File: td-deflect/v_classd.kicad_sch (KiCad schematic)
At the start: 34 parts, among them J8 Conn_01x02_Male, Q15 BSC600N25NS3GATMA1CT-ND, Q16 BSC600N25NS3GATMA1CT-ND, Q20 BSC600N25NS3GATMA1CT-ND, Q21 BSC600N25NS3GATMA1CT-ND, U34 IRS2005S, U35 IRS2005S, U36 MAX9919F, U37 MAX9919F

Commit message: fix drc errors
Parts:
- J8: symbol Connector:Conn_01x02_Male -> Connector:Conn_01x02_Pin
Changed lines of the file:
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@@
     )
   )
-  (symbol (lib_id "Connector:Conn_01x02_Male") (at 190.5 77.47 0) (mirror y) (unit 1)
+  (symbol (lib_id "Connector:Conn_01x02_Pin") (at 190.5 77.47 0) (mirror y) (unit 1)
     (in_bom yes) (on_board yes) (dnp no)
     (property "Reference" "J8" (at 187.7568 72.8726 0)

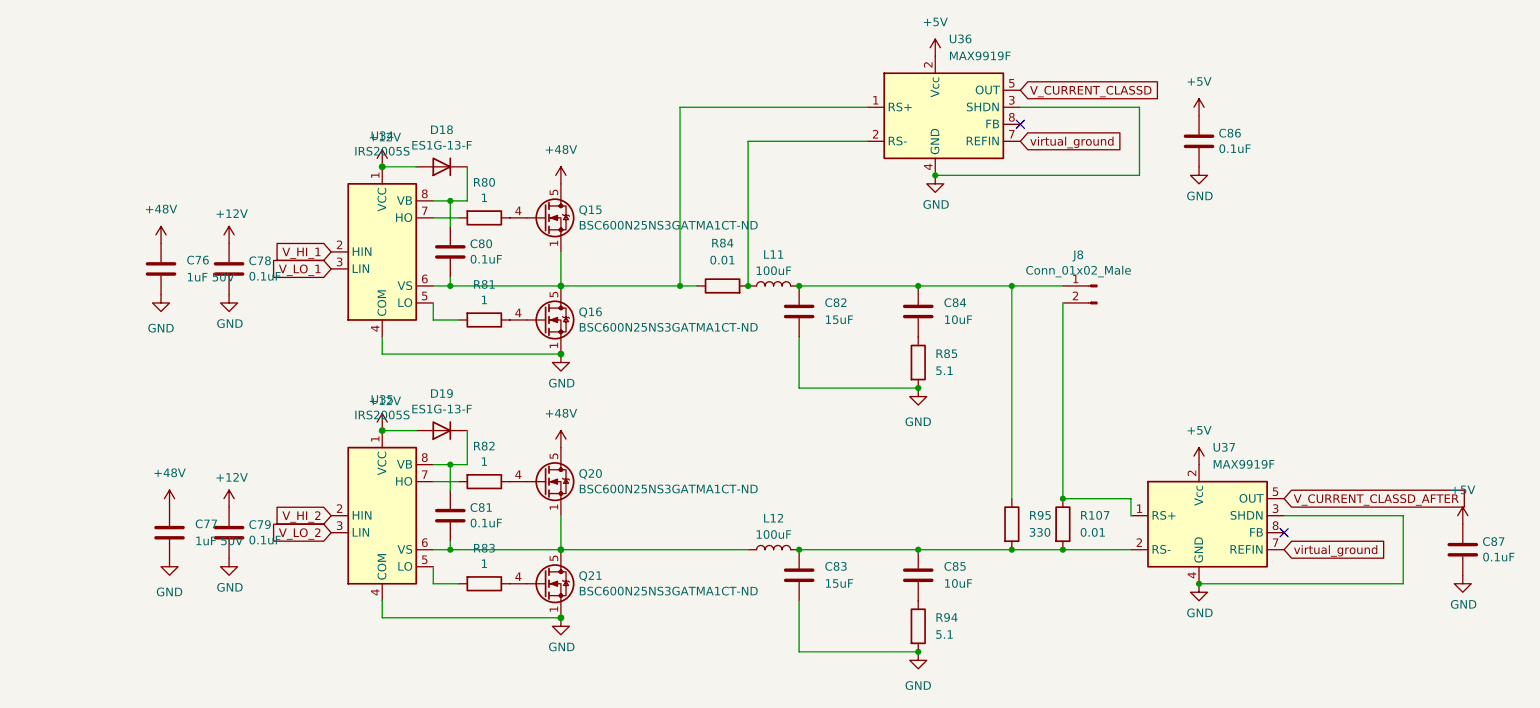
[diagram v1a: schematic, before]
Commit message: fix remaining erc errors
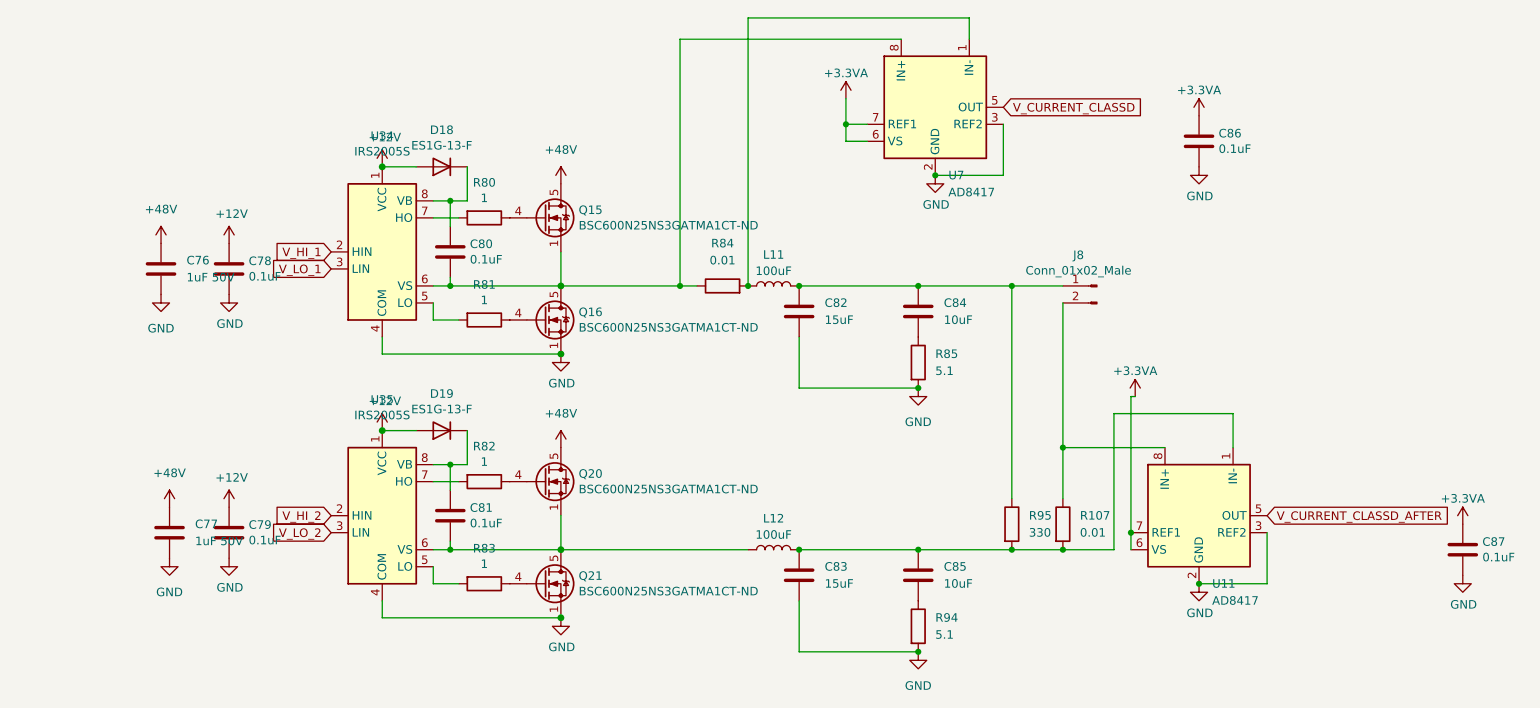
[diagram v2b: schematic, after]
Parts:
- removed U36, U37: MAX9919F, Package_SO:SOIC-8-1EP_3.9x4.9mm_P1.27mm_EP2.41x3.3mm, symbol td-crt:MAX9919F
- added U11, U7: AD8417, symbol Amplifier_Current:AD8417
- D18, D19: footprint Diode_SMD:D_SMA -> Diode_THT:D_DO-41_SOD81_P10.16mm_Horizontal
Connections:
- net GND: now also U11.2 (GND), U11.3 (REF2), U7.2 (GND), U7.3 (REF2)
- net V_CURRENT_CLASSD: now also U7.5 (OUT)
- net V_CURRENT_CLASSD_AFTER: now also U11.5 (OUT)
- net at C83.1, C85.1, L12.2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: now also U11.1 (IN-)
- net at C80.2, Q15.1 (S), Q15.2 (S)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: now also U7.8 (IN+)
- net at L11.1, R84.2: now also U7.1 (IN-)
- net at J8.2 (Pin_2), R107.1: now also U11.8 (IN+)
- net +5V renamed +3.3VA
- net +3.3VA: now also U11.6 (VS), U11.7 (REF1), U7.6 (VS), U7.7 (REF1)
- no-connect marks 2 -> 0

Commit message: more layout work
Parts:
- D18, D19: value ES1G-13-F -> 1N4148W-TP; footprint Diode_THT:D_DO-41_SOD81_P10.16mm_Horizontal -> Diode_SMD:D_SOD-123; Digikey ES1G-FDICT-ND -> 1N4148WTPMSCT-ND
- U11, U7: footprint (none) -> Package_SO:SOIC-8_3.9x4.9mm_P1.27mm
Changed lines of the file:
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@@
       (effects (font (size 1.27 1.27)))
     )
-    (property "Value" "ES1G-13-F" (at 92.71 56.515 0)
-      (effects (font (size 1.27 1.27)))
-    )
-    (property "Footprint" "Diode_THT:D_DO-41_SOD81_P10.16mm_Horizontal" (at 92.71 55.245 0)
+    (property "Value" "1N4148W-TP" (at 92.71 56.515 0)
+      (effects (font (size 1.27 1.27)))
+    )
+    (property "Footprint" "Diode_SMD:D_SOD-123" (at 92.71 55.245 0)
       (effects (font (size 1.27 1.27)) hide)
     )
@@
       (effects (font (size 1.27 1.27)) hide)
     )
-    (property "Digikey" "ES1G-FDICT-ND" (at 92.71 59.69 0)
+    (property "Digikey" "1N4148WTPMSCT-ND" (at 92.71 59.69 0)
       (effects (font (size 1.27 1.27)) hide)
     )
@@
       (effects (font (size 1.27 1.27)))
     )
-    (property "Value" "ES1G-13-F" (at 92.71 95.885 0)
-      (effects (font (size 1.27 1.27)))
-    )
-    (property "Footprint" "Diode_THT:D_DO-41_SOD81_P10.16mm_Horizontal" (at 92.71 94.615 0)
+    (property "Value" "1N4148W-TP" (at 92.71 95.885 0)
+      (effects (font (size 1.27 1.27)))
+    )
+    (property "Footprint" "Diode_SMD:D_SOD-123" (at 92.71 94.615 0)
       (effects (font (size 1.27 1.27)) hide)
     )
@@
       (effects (font (size 1.27 1.27)) hide)
     )
-    (property "Digikey" "ES1G-FDICT-ND" (at 92.71 99.06 0)
+    (property "Digikey" "1N4148WTPMSCT-ND" (at 92.71 99.06 0)
       (effects (font (size 1.27 1.27)) hide)
     )
@@
       (effects (font (size 1.27 1.27)) (justify left))
     )
-    (property "Footprint" "" (at 167.64 59.69 0)
+    (property "Footprint" "Package_SO:SOIC-8_3.9x4.9mm_P1.27mm" (at 167.64 59.69 0)
       (effects (font (size 1.27 1.27)) hide)
     )
@@
       (effects (font (size 1.27 1.27)) (justify left))
     )
-    (property "Footprint" "" (at 207.01 120.65 0)
-      (effects (font (size 1.27 1.27)) hide)
-    )
+    (property "Footprint" "Package_SO:SOIC-8_3.9x4.9mm_P1.27mm" (at 207.01 120.65 0)
+      (effects (font (size 1.27 1.27)) hide)
+    )

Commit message: more layout
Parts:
- renumbered C76 to C501, C77 to C502, C78 to C503, C79 to C504, C80 to C505, C81 to C506, C82 to C507, C83 to C508, C84 to C509, C85 to C510, C86 to C511, C87 to C512, D18 to D501, D19 to D502, J8 to J501, L11 to L501, L12 to L502, Q15 to Q501, Q16 to Q502, Q20 to Q503, Q21 to Q504, R80 to R501, R81 to R502, R82 to R503, R83 to R504, R84 to R505, R85 to R506, R94 to R507, R95 to R508, R107 to R509, U34 to U501, U35 to U502, U7 to U503, U11 to U504

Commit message: update pcb
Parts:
- C501, C502: Digikey (none) -> 13-CC0805KFX7R9BB105CT-ND
- C503, C504, C505, C506, C511, C512: Digikey 1276-1099-1-ND -> 311-1140-1-ND
- C507, C508: Digikey (none) -> 445-14423-1-ND
- C509, C510: Digikey (none) -> 490-18663-1-ND
- J501: Digikey (none) -> DNP
- L501, L502: value 100uF -> 100uH; Digikey (none) -> 4044-CSAB1260A-101MCT-ND
- Q501, Q502, Q503, Q504: Digikey BSZ42DN25NS3GATMA1CT-ND -> BSC600N25NS3GATMA1CT-ND
- R505, R509: Digikey (none) -> 311-0.01NUCT-ND
- R506, R507: Digikey (none) -> 311-5.1ARCT-ND
- R508: Digikey (none) -> 13-RC0805FR-13330RLCT-ND
- U503, U504: Digikey (none) -> 505-AD8417WBRZ-ND
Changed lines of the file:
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@@
+      (effects (font (size 1.27 1.27)) hide)
+    )
+    (property "Digikey" "311-5.1ARCT-ND" (at 163.83 88.9 0)
       (effects (font (size 1.27 1.27)) hide)
     )
@@
       (effects (font (size 1.27 1.27)))
     )
-    (property "Value" "100uF" (at 142.24 114.6146 90)
+    (property "Value" "100uH" (at 142.24 114.6146 90)
       (effects (font (size 1.27 1.27)))
     )
@@
       (effects (font (size 1.27 1.27)) hide)
     )
+    (property "Digikey" "4044-CSAB1260A-101MCT-ND" (at 142.24 116.84 0)
+      (effects (font (size 1.27 1.27)) hide)
+    )
     (pin "1")
     (pin "2")
@@
       (effects (font (size 1.27 1.27)) hide)
     )
-    (property "Digikey" "1276-1099-1-ND" (at 60.96 114.3 0)
+    (property "Digikey" "311-1140-1-ND" (at 60.96 114.3 0)
       (effects (font (size 1.27 1.27)) hide)
     )
@@
     )
     (property "Datasheet" "~" (at 52.07 114.3 0)
+      (effects (font (size 1.27 1.27)) hide)
+    )
+    (property "Digikey" "13-CC0805KFX7R9BB105CT-ND" (at 52.07 114.3 0)
       (effects (font (size 1.27 1.27)) hide)
     )
@@
       (effects (font (size 1.27 1.27)) (justify left) hide)
     )
-    (property "Digikey" "BSZ42DN25NS3GATMA1CT-ND" (at 107.95 106.68 0)
+    (property "Digikey" "BSC600N25NS3GATMA1CT-ND" (at 107.95 106.68 0)
       (effects (font (size 1.27 1.27)) hide)
     )
@@
       (effects (font (size 1.27 1.27)) hide)
     )
-    (property "Digikey" "1276-1099-1-ND" (at 245.11 116.84 0)
+    (property "Digikey" "311-1140-1-ND" (at 245.11 116.84 0)
       (effects (font (size 1.27 1.27)) hide)
     )
@@
     )
     (property "Datasheet" "~" (at 134.62 77.47 0)
+      (effects (font (size 1.27 1.27)) hide)
+    )
+    (property "Digikey" "311-0.01NUCT-ND" (at 134.62 77.47 0)
       (effects (font (size 1.27 1.27)) hide)
     )
@@
       (effects (font (size 1.27 1.27)) (justify left) hide)
     )
-    (property "Digikey" "BSZ42DN25NS3GATMA1CT-ND" (at 107.95 121.92 0)
+    (property "Digikey" "BSC600N25NS3GATMA1CT-ND" (at 107.95 121.92 0)
       (effects (font (size 1.27 1.27)) hide)
     )
@@
       (effects (font (size 1.27 1.27)) hide)
     )
+    (property "Digikey" "13-RC0805FR-13330RLCT-ND" (at 177.8 113.03 0)
+      (effects (font (size 1.27 1.27)) hide)
+    )
     (pin "1")
     (pin "2")
@@
       (effects (font (size 1.27 1.27)) hide)
     )
+    (property "Digikey" "490-18663-1-ND" (at 163.83 120.65 0)
+      (effects (font (size 1.27 1.27)) hide)
+    )
     (pin "1")
     (pin "2")
@@
       (effects (font (size 1.27 1.27)) hide)
     )
+    (property "Digikey" "490-18663-1-ND" (at 163.83 81.28 0)
+      (effects (font (size 1.27 1.27)) hide)
+    )
     (pin "1")
     (pin "2")
@@
       (effects (font (size 1.27 1.27)) hide)
     )
+    (property "Digikey" "13-CC0805KFX7R9BB105CT-ND" (at 50.8 74.93 0)
+      (effects (font (size 1.27 1.27)) hide)
+    )
     (pin "1")
     (pin "2")
@@
       (effects (font (size 1.27 1.27)) hide)
     )
-    (property "Digikey" "1276-1099-1-ND" (at 60.96 74.93 0)
+    (property "Digikey" "311-1140-1-ND" (at 60.96 74.93 0)
       (effects (font (size 1.27 1.27)) hide)
     )
@@
       (effects (font (size 1.27 1.27)) hide)
     )
+    (property "Digikey" "445-14423-1-ND" (at 146.05 81.28 0)
+      (effects (font (size 1.27 1.27)) hide)
+    )
     (pin "1")
     (pin "2")
@@
     )
     (property "Datasheet" "https://www.analog.com/media/en/technical-documentation/data-sheets/AD8417.pdf" (at 182.88 68.58 0)
+      (effects (font (size 1.27 1.27)) hide)
+    )
+    (property "Digikey" "505-AD8417WBRZ-ND" (at 166.37 50.8 0)
       (effects (font (size 1.27 1.27)) hide)
     )
@@
       (effects (font (size 1.27 1.27)) hide)
     )
-    (property "Digikey" "1276-1099-1-ND" (at 205.74 55.88 0)
+    (property "Digikey" "311-1140-1-ND" (at 205.74 55.88 0)
       (effects (font (size 1.27 1.27)) hide)
     )
@@
       (effects (font (size 1.27 1.27)) hide)
     )
-    (property "Digikey" "1276-1099-1-ND" (at 93.98 72.39 0)
+    (property "Digikey" "311-1140-1-ND" (at 93.98 72.39 0)
       (effects (font (size 1.27 1.27)) hide)
     )
@@
     )
     (property "Datasheet" "~" (at 185.42 113.03 0)
+      (effects (font (size 1.27 1.27)) hide)
+    )
+    (property "Digikey" "311-0.01NUCT-ND" (at 185.42 113.03 0)
       (effects (font (size 1.27 1.27)) hide)
     )
@@
       (effects (font (size 1.27 1.27)) (justify left) hide)
     )
-    (property "Digikey" "BSZ42DN25NS3GATMA1CT-ND" (at 107.95 67.31 0)
+    (property "Digikey" "BSC600N25NS3GATMA1CT-ND" (at 107.95 67.31 0)
       (effects (font (size 1.27 1.27)) hide)
     )
@@
       (effects (font (size 1.27 1.27)) (justify left) hide)
     )
-    (property "Digikey" "BSZ42DN25NS3GATMA1CT-ND" (at 107.95 82.55 0)
+    (property "Digikey" "BSC600N25NS3GATMA1CT-ND" (at 107.95 82.55 0)
       (effects (font (size 1.27 1.27)) hide)
     )
@@
       (effects (font (size 1.27 1.27)) hide)
     )
+    (property "Digikey" "DNP" (at 190.5 77.47 0)
+      (effects (font (size 1.27 1.27)) hide)
+    )
     (pin "1")
     (pin "2")
@@
       (effects (font (size 1.27 1.27)) hide)
     )
+    (property "Digikey" "445-14423-1-ND" (at 146.05 120.65 0)
+      (effects (font (size 1.27 1.27)) hide)
+    )
     (pin "1")
     (pin "2")
@@
       (effects (font (size 1.27 1.27)))
     )
-    (property "Value" "100uF" (at 142.24 75.2446 90)
+    (property "Value" "100uH" (at 142.24 75.2446 90)
       (effects (font (size 1.27 1.27)))
     )
@@
       (effects (font (size 1.27 1.27)) hide)
     )
+    (property "Digikey" "4044-CSAB1260A-101MCT-ND" (at 142.24 77.47 0)
+      (effects (font (size 1.27 1.27)) hide)
+    )
     (pin "1")
     (pin "2")
@@
       (effects (font (size 1.27 1.27)) hide)
     )
-    (property "Digikey" "1276-1099-1-ND" (at 93.98 111.76 0)
+    (property "Digikey" "311-1140-1-ND" (at 93.98 111.76 0)
       (effects (font (size 1.27 1.27)) hide)
     )
@@
       (effects (font (size 1.27 1.27)) hide)
     )
+    (property "Digikey" "311-5.1ARCT-ND" (at 163.83 128.27 0)
+      (effects (font (size 1.27 1.27)) hide)
+    )
     (pin "1")
     (pin "2")
@@
       (effects (font (size 1.27 1.27)) hide)
     )
+    (property "Digikey" "505-AD8417WBRZ-ND" (at 205.74 111.76 0)
+      (effects (font (size 1.27 1.27)) hide)
+    )

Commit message: finish board
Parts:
- C507, C508: footprint Capacitor_SMD:C_0805_2012Metric_Pad1.18x1.45mm_HandSolder -> Capacitor_SMD:C_Elec_6.3x7.7; Digikey 445-14423-1-ND -> 565-HHXD500ARA150MF80GCT-ND
- C509, C510: footprint Capacitor_SMD:C_0805_2012Metric_Pad1.18x1.45mm_HandSolder -> Capacitor_SMD:C_Elec_6.3x5.8; Digikey 490-18663-1-ND -> 565-4781-1-ND
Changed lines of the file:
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@@
 			)
 		)
-		(property "Footprint" "Capacitor_SMD:C_0805_2012Metric_Pad1.18x1.45mm_HandSolder"
+		(property "Footprint" "Capacitor_SMD:C_Elec_6.3x5.8"
 			(at 164.7952 124.46 0)
 			(effects
@@
 			)
 		)
-		(property "Digikey" "490-18663-1-ND"
+		(property "Digikey" "565-4781-1-ND"
 			(at 163.83 120.65 0)
 			(effects
@@
 			)
 		)
-		(property "Footprint" "Capacitor_SMD:C_0805_2012Metric_Pad1.18x1.45mm_HandSolder"
+		(property "Footprint" "Capacitor_SMD:C_Elec_6.3x5.8"
 			(at 164.7952 85.09 0)
 			(effects
@@
 			)
 		)
-		(property "Digikey" "490-18663-1-ND"
+		(property "Digikey" "565-4781-1-ND"
 			(at 163.83 81.28 0)
 			(effects
@@
 			)
 		)
-		(property "Footprint" "Capacitor_SMD:C_0805_2012Metric_Pad1.18x1.45mm_HandSolder"
+		(property "Footprint" "Capacitor_SMD:C_Elec_6.3x7.7"
 			(at 147.0152 85.09 0)
 			(effects
@@
 			)
 		)
-		(property "Digikey" "445-14423-1-ND"
+		(property "Digikey" "565-HHXD500ARA150MF80GCT-ND"
 			(at 146.05 81.28 0)
 			(effects
@@
 			)
 		)
-		(property "Footprint" "Capacitor_SMD:C_0805_2012Metric_Pad1.18x1.45mm_HandSolder"
+		(property "Footprint" "Capacitor_SMD:C_Elec_6.3x7.7"
 			(at 147.0152 124.46 0)
 			(effects
@@
 			)
 		)
-		(property "Digikey" "445-14423-1-ND"
+		(property "Digikey" "565-HHXD500ARA150MF80GCT-ND"
 			(at 146.05 120.65 0)
 			(effects

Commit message: bunch of random updates
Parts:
- added C28, C29: 100uF 50V, symbol Device:C_Polarized
- D501, D502: now not fitted
- Q501, Q502, Q503, Q504: value BSC600N25NS3GATMA1CT-ND -> BSC340N08NS3GATMA1; Digikey BSC600N25NS3GATMA1CT-ND -> BSC340N08NS3GATMA1CT-ND
- U501, U502: value IRS2005S -> 2ED2101S06FXUMA1; Digikey IRS2005STRPBFCT-ND -> 448-2ED2101S06FXUMA1CT-ND
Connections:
- net +48V: now also C28.1, C29.1
- net GND: now also C28.2, C29.2
